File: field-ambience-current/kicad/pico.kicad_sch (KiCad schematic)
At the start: 9 parts, among them J4 SWD 1.27mm (SWCLK/GND/SWDIO), SW11 Reset 6mm SMD, SW12 BOOTSEL 6mm SMD (DNP for THT-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, U1 Raspberry_Pi_Pico2 (RP2350)

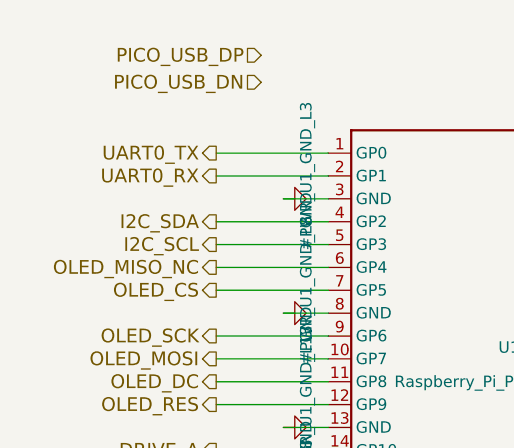
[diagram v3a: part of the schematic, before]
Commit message: v0.6.3-r2: PAM8403 SHDN/MUTE pull-downs + UART naming + TODO list
Addresses 2nd-iteration ChatGPT review findings (most that don't need
KiCad GUI). All TODO items documented in PCB_TODO.md.

B4: PAM8403H /SHDN and /MUTE hardware pull-downs
- R_MUTE_PD 10k from pin 5 (/MUTE) to GND
- R_SHDN_PD 10k from pin 12 (/SHDN) to GND
- Default state during Pico boot/reset = both LOW = Amp OFF + MUTED
- Pico firmware drives HIGH only after power-sequencing per SPEC §5
- Prevents undefined Amp state during boot transients (pop/click safety)

I7: UART net naming disambiguated
- Old: UART0_TX / UART0_RX (perspective-ambiguous)
- New:
  - PICO_TX_PI_RX (Pico GP0 → Pi GPIO15 pin 10)
  - PI_TX_PICO_RX (Pi GPIO14 pin 8 → R1 1k → Pico GP1)
- Changed in pico_sheet, pi_sheet, root_sheet (pins + labels)

N4: Titleblock revs synced
- audio.kicad_sch: v0.6.1 → v0.6.3
- power_tree.kicad_sch: v0.6 → v0.6.3
- Comments updated to reflect current state

N5: Stale comments cleanup
- power_tree_sheet: USB-C pin-number references updated to USB-C spec
- audio_sheet: PAM8403 references updated to PAM8403H + PDF reference
- BLOCKER-comment in audio sheet replaced with "boot-safe pull-downs added"

New PCB_TODO.md tracks remaining items for PCB-layout readiness:
- BLOCKER (4): need KiCad GUI — footprint verification, ERC report
- IMPORTANT (7): power budget recalc, mech coords, BOM split, etc.
- NICE-TO-HAVE (5): XSMT via GPIO, I²S series R, etc.

Analyzer status: 0 functional errors (same 3 VM-001 false positives),
19 warnings, 87 components (was 85, +2 for pull-downs), 117 nets.

Verified via analyzer pin_nets:
- R_MUTE_PD: pin1=AMP_MUTE, pin2=GND ✓
- R_SHDN_PD: pin1=AMP_SHUTDOWN, pin2=GND ✓
- U1 Pin 1 (GP0) = PICO_TX_PI_RX ✓
- U1 Pin 2 (GP1) = PI_TX_PICO_RX ✓
- U4 Pin 5 (MUTE) = AMP_MUTE ✓
- U4 Pin 12 (SHDN) = AMP_SHUTDOWN ✓

Note on reviewer's USB-C claim: Reviewer indicated USB-C symbol still
has wrong pinout in PR. Verified via GitHub API that PR HEAD (commit
5ca0bcb) has the correct mapping (VB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
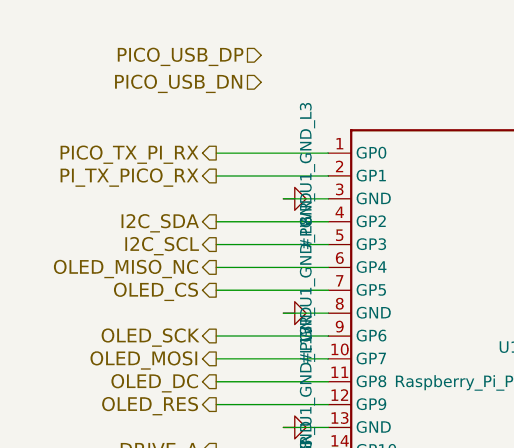
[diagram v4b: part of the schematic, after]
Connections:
- net UART0_RX renamed PI_TX_PICO_RX
- net UART0_TX renamed PICO_TX_PI_RX
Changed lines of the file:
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@@
     (effects (font (size 1.524 1.524)) (justify right))
 )
-  (hierarchical_label "UART0_TX" (shape output) (at 70 75.87 0)
+  (hierarchical_label "PICO_TX_PI_RX" (shape output) (at 70 75.87 0)
     (effects (font (size 1.524 1.524)) (justify right))
 )
-  (hierarchical_label "UART0_RX" (shape output) (at 70 78.41000000000001 0)
+  (hierarchical_label "PI_TX_PICO_RX" (shape output) (at 70 78.41000000000001 0)
     (effects (font (size 1.524 1.524)) (justify right))
 )

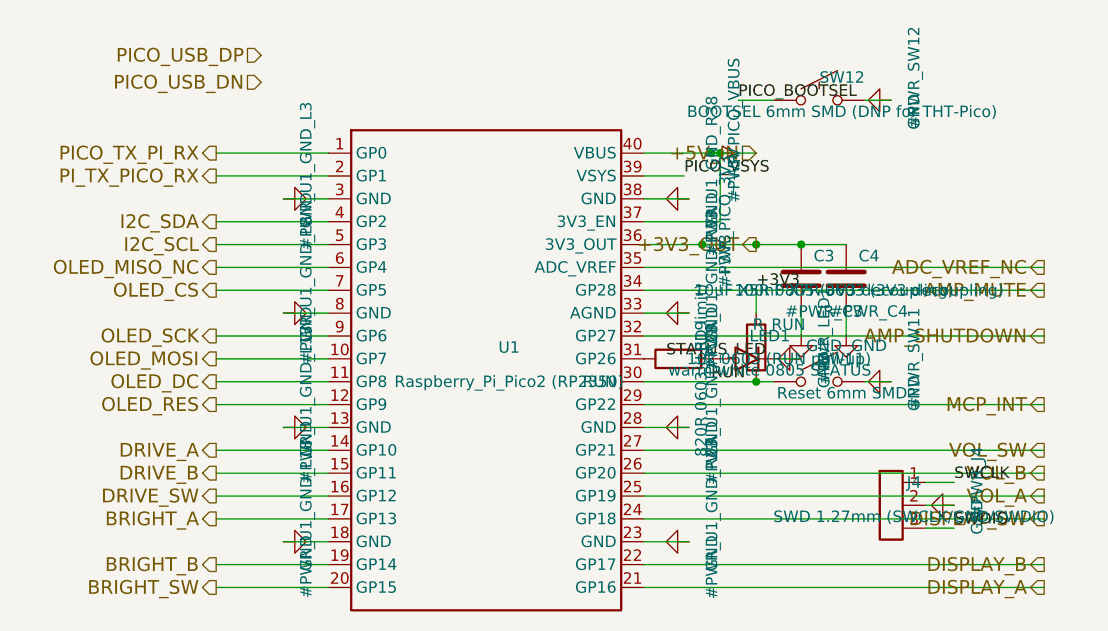
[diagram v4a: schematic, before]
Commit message: v0.6.3-r6: Stabilization pass — PVDD decoupling, startup sequence, SPEC consolidation
No new features. Pure stabilization per senior-engineer review.

=== HIGH fixes ===

1. PAM8403H PVDD decoupling (pins 4, 13) — was missing
   Datasheet (PAM8403H.PDF "Application Information") requires:
   "1.0µF ceramic close to VDD" (HF) + "20µF or greater" (bulk).
   Previous: only C9 10µF + C9b 100nF at VDD (pin 6). PVDD pins 4 (L)
   and 13 (R) had no local decoupling → Class-D 250kHz switching
   transients would modulate PVDD → distortion at volume + EMI.
   Fix:
   - Left (VDD pin6 + PVDD-L pin4): C9 10µF→22µF (C45783), C9b 100nF→1µF
   - Right (PVDD-R pin13): NEW C_PVDDR 22µF + C_PVDDR_HF 1µF local
   Note: corrected my own earlier review — PVDD is pins 4+13 only,
   NOT 4/10/13 (pin 10 is INR input, not power).

2. PAM8403 startup sequence — was in wrong order in SPEC
   SPEC §8 had: /MUTE=HIGH first, then /SHDN=HIGH 100ms later.
   Both are active-LOW. Un-muting before chip wakeup means audio
   passes the instant /SHDN goes HIGH → pop.
   Fix: /SHDN=HIGH first (chip wakes, references settle, output still
   muted via /MUTE=LOW), then /MUTE=HIGH 50ms later. Shutdown reverses.
   Corrected in SPEC §5 AND §8 body (not just errata).

=== SPEC consolidation (single source of truth) ===

- Moved entire Errata-Historie (v0.6.1 → v0.6.3-r5, 327 lines) out of
  SPEC body into new CHANGELOG.md
- SPEC header rewritten: clean rev marker, status "SCHEMATIC IN REVIEW"
- SPEC body now describes ONLY the current state, no errata/old-value
  contradictions
- §3 decoupling table updated: C9 22µF, C9b 1µF, + C_PVDDR/C_PVDDR_HF,
  + C_VREF rows added
- §5 + §8: startup sequence corrected, active-low convention documented

=== Cross-domain fix: AMP signal naming ===

Renamed AMP_SHUTDOWN → AMP_nSHDN, AMP_MUTE → AMP_nMUTE throughout the
generator (17 occurrences). Both PAM8403H /SHDN and /MUTE are active-LOW;
old names implied active-high and were a firmware-bug magnet. SPEC §5
already used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
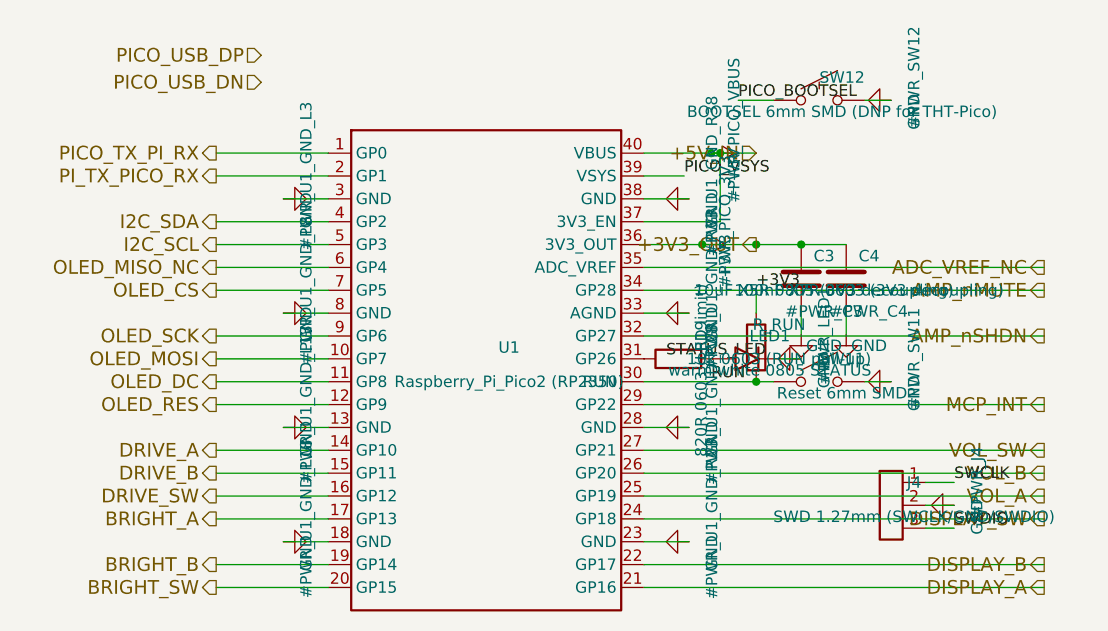
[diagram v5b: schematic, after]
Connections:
- net AMP_MUTE renamed AMP_nMUTE
- net AMP_SHUTDOWN renamed AMP_nSHDN
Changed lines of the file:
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@@
     (effects (font (size 1.524 1.524)) (justify right))
 )
-  (hierarchical_label "AMP_SHUTDOWN" (shape output) (at 162 96.19 180)
+  (hierarchical_label "AMP_nSHDN" (shape output) (at 162 96.19 180)
     (effects (font (size 1.524 1.524)) (justify right))
 )
-  (hierarchical_label "AMP_MUTE" (shape output) (at 162 91.11 180)
+  (hierarchical_label "AMP_nMUTE" (shape output) (at 162 91.11 180)
     (effects (font (size 1.524 1.524)) (justify right))
 )

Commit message: fix(bom): make entire BOM correctly JLC-orderable — 7 real part errors fixed
Verified every LCSC number against jlcsearch for existence, stock, AND that
it resolves to the intended value/package. Found 7 parts that would have
built WRONG or were unorderable:

CRITICAL value/package errors (LCSC pointed at the wrong part):
- R_VOL_L/R: C25092 = 22ohm 0402  -> C4184  (real 20k 0603, Basic).
  Was wrong value AND footprint; would have wrecked the PAM8403 input gain.
- R_LO_L/R:  C22962 = 220ohm       -> C23345 (real 22ohm 0603, Basic).
- R_BCK/LRCK/DOUT: C23138 = 330ohm -> C23140 (real 33ohm 0603, Basic).

Unorderable -> assigned real in-stock parts:
- J8 jack:  C2884109 (nonexistent) -> C431535 (PJ-320D SMD).
- C_BULK:   placeholder            -> C46550395 (1000uF 16V SMD D10x10.5).
- LED1:     no LCSC                -> C965818 (white 0805).
- R1:       C22548 Extended        -> C21190 Basic (prior commit).

Also aligned all MPN text to the actual LCSC part (Yageo text vs Uni Royal/
Samsung parts JLC ships) so the BOM is internally consistent.

Re-verified: 25 distinct LCSC, all in stock, ZERO value/package mismatches,
14 Basic / 11 Extended. SPEC §4 stale refs (C_BULK/J8/R_LO) updated.
MEINE_TODO Abschnitt 0 rewritten with the full orderability result.

Self-supply parts (Pico, OLED, speakers, Choc sockets, EC11, headers) keep
no LCSC by design — JLC cannot assemble those.

https://claude.ai/code/session_01K5kLTFpDCCoYwx2dq6RkAv
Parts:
- LED1: LCSC TBD -> C965818; MPN Generic warm-white 2700K -> XL-2012UWC (white 0805)
- R19: MPN RC0603FR-07820RL -> 0603WAF8200T5E
- R_RUN: MPN RC0603FR-0710KL -> 0603WAF1002T5E
- SW11, SW12: MPN TL3342F160QG -> TS-1088-AR02016
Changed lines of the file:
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@@
       (property "Datasheet" "~" (at 130 97.46 0)
         (effects (font (size 1.27 1.27)) hide))
-      (property "MPN" "RC0603FR-0710KL" (at 132.54 101.27 0)
+      (property "MPN" "0603WAF1002T5E" (at 132.54 101.27 0)
         (effects (font (size 1.27 1.27)) hide))
       (property "LCSC" "C25804" (at 132.54 102.53999999999999 0)
@@
       (property "Datasheet" "~" (at 137 101.27000000000001 0)
         (effects (font (size 1.27 1.27)) hide))
-      (property "MPN" "TL3342F160QG" (at 139.54 105.08000000000001 0)
+      (property "MPN" "TS-1088-AR02016" (at 139.54 105.08000000000001 0)
         (effects (font (size 1.27 1.27)) hide))
       (property "LCSC" "C720477" (at 139.54 106.35000000000001 0)
@@
       (property "Datasheet" "~" (at 121.35 98.73 0)
         (effects (font (size 1.27 1.27)) hide))
-      (property "MPN" "RC0603FR-07820RL" (at 123.89 102.54 0)
+      (property "MPN" "0603WAF8200T5E" (at 123.89 102.54 0)
         (effects (font (size 1.27 1.27)) hide))
       (property "LCSC" "C23253" (at 123.89 103.81 0)
@@
       (property "Datasheet" "~" (at 128.97 98.73 0)
         (effects (font (size 1.27 1.27)) hide))
-      (property "MPN" "Generic warm-white 2700K" (at 131.51 102.54 0)
+      (property "MPN" "XL-2012UWC (white 0805)" (at 131.51 102.54 0)
         (effects (font (size 1.27 1.27)) hide))
-      (property "LCSC" "TBD" (at 131.51 103.81 0)
+      (property "LCSC" "C965818" (at 131.51 103.81 0)
         (effects (font (size 1.27 1.27)) hide))
     (instances
@@
       (property "Datasheet" "~" (at 137 70 0)
         (effects (font (size 1.27 1.27)) hide))
-      (property "MPN" "TL3342F160QG" (at 139.54 73.81 0)
+      (property "MPN" "TS-1088-AR02016" (at 139.54 73.81 0)
         (effects (font (size 1.27 1.27)) hide))
       (property "LCSC" "C720477" (at 139.54 75.08 0)
